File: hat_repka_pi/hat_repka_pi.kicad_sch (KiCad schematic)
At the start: 3 parts, among them Q1 BD233

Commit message: Добавлены основные компоненты на плату
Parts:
- removed C1: C_Small, symbol Device:C_Small
- removed Q1: BD233, Package_TO_SOT_THT:TO-126-3_Vertical, symbol Transistor_BJT:BD233
- removed R1: R, symbol Device:R
- added DS1: MT-12864J-2VLW-3V0, Display:MT-12864J-2VLW-3V0, symbol Melt:MT-12864J-2VLW-3V0
- added J1: Repka_Pi_3_type_piout_1, symbol Repka-Pi3:Repka_Pi_3_type_piout_1
- added Q1: 2SC1815, Package_TO_SOT_THT:TO-92_Inline, symbol Transistor_BJT:2SC1815
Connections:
- new net: DS1.1 (3.3V), DS1.20 (LEDK/EL), J1.1 (3V3)
- new net: DS1.10 (DB6), J1.19 (PC0/64/GPIO)
- new net: DS1.11 (DB7), J1.21 (PC1/65/GPIO)
- new net: DS1.12 (~{CS1}), J1.23 (PC2/66/GPIO)
- new net: DS1.13 (~{CS2}), J1.27 (PA19/19/GPIO)
- new net: DS1.14 (~{RST}), J1.29 (PA0/0/GPIO)
- new net: DS1.15 (R/~{W}), DS1.19 (LEDA/EL), DS1.2 (GND), J1.6 (GND)
- new net: DS1.16 (D/~{I}), J1.31 (PA1/1/GPIO)
- new net: DS1.17 (E), J1.33 (PL10/362/GPIO)
- new net: DS1.4 (DB0), J1.3 (PA12/12/GPIO)
- new net: DS1.5 (DB1), J1.5 (PA11/11/GPIO)
- new net: DS1.6 (DB2), J1.7 (PA7/7/GPIO)
- new net: DS1.7 (DB3), J1.11 (PA8/8/GPIO)
- new net: DS1.8 (DB4), J1.13 (PA9/9/GPIO)
- new net: DS1.9 (DB5), J1.15 (PA10/10/GPIO)

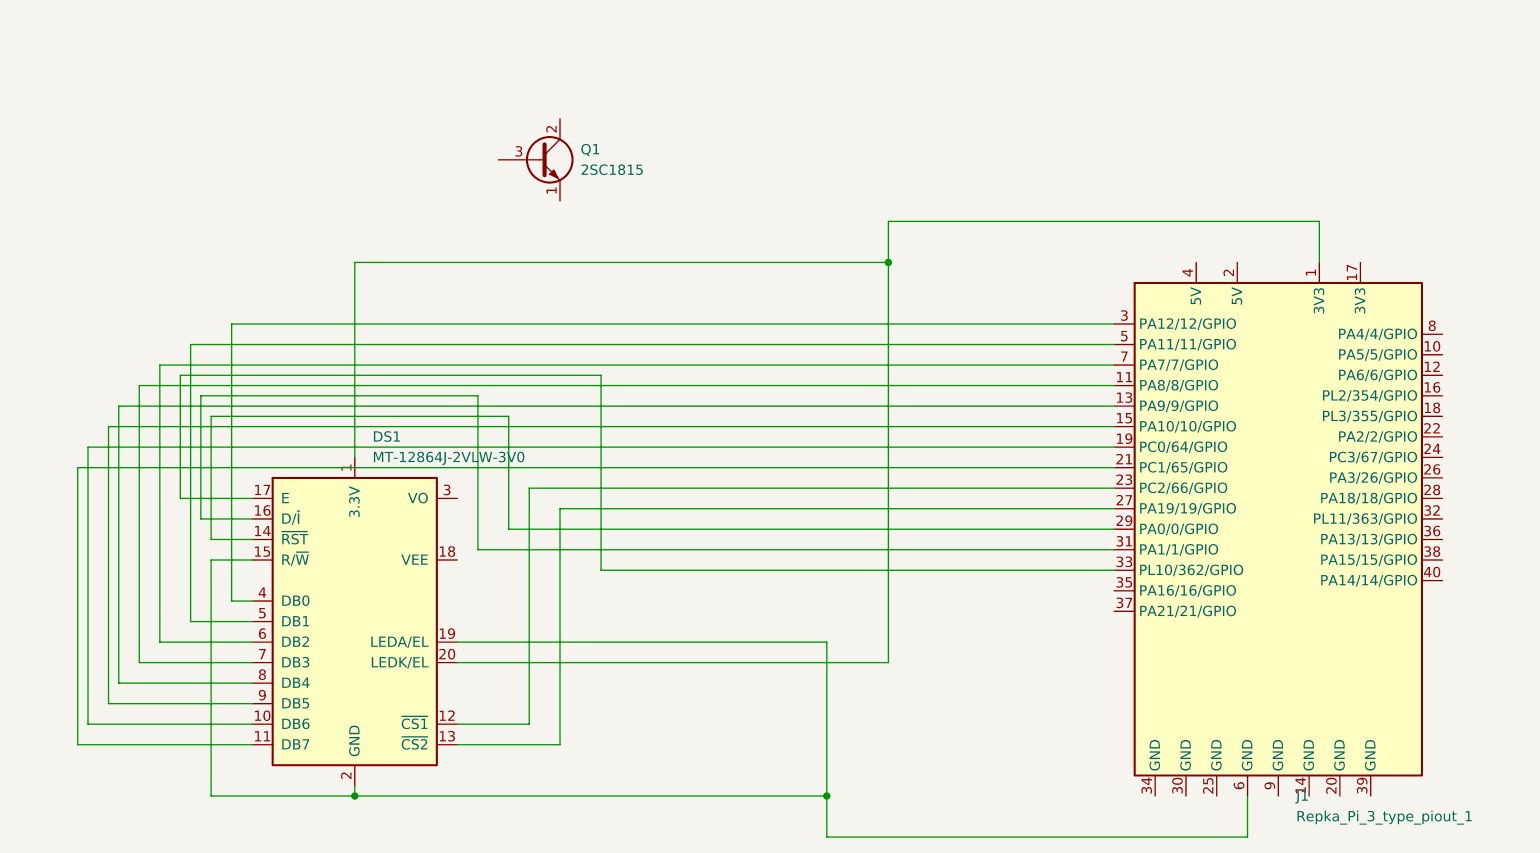
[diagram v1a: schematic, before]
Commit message: // Добавлена возможность подключить внешний дисплей ks0108 с паралельным интерфейсом
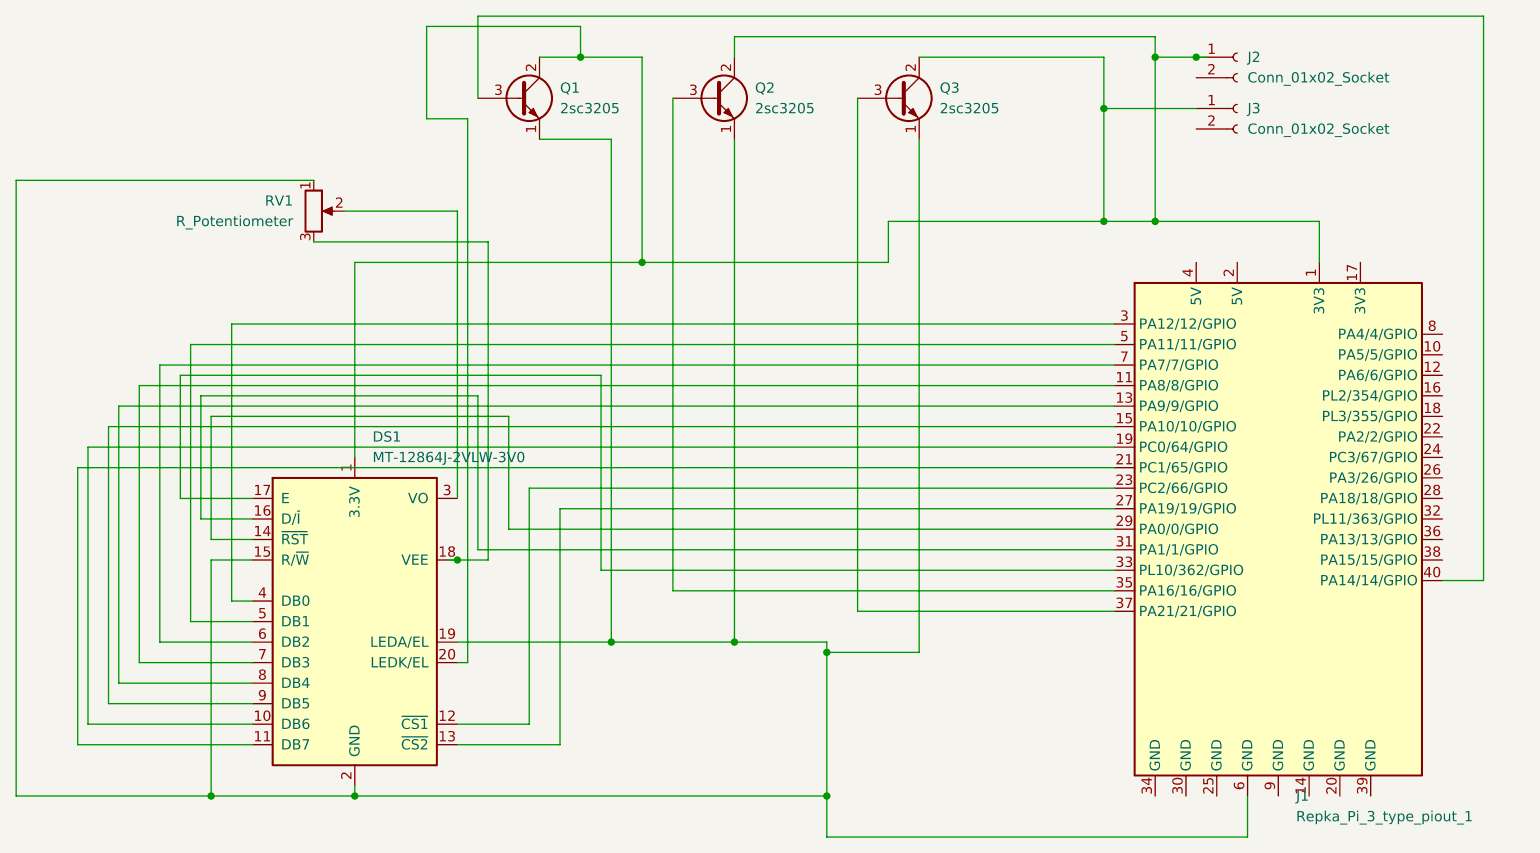
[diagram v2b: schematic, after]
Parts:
- removed Q1: 2SC1815, Package_TO_SOT_THT:TO-92_Inline, symbol Transistor_BJT:2SC1815
- added J2: Conn_01x02_Socket, Connector_PinSocket_2.54mm:PinSocket_1x02_P2.54mm_Vertical, symbol Connector:Conn_01x02_Socket
- added J3: Conn_01x02_Socket, symbol Connector:Conn_01x02_Socket
- added Q1, Q2, Q3: 2sc3205, Package_TO_SOT_THT:TO-92_Inline, symbol Other:2SC1815
- added RV1: R_Potentiometer, Potentiometer_THT:Potentiometer_Bourns_3296Y_Vertical, symbol Device:R_Potentiometer
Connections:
- net at DS1.1 (3.3V), DS1.20 (LEDK/EL), J1.1 (3V3): now also J2.1 (Pin_1), J3.1 (Pin_1), Q1.2 (C), Q2.2 (C), Q3.2 (C)
- net at DS1.15 (R/~{W}), DS1.19 (LEDA/EL), DS1.2 (GND)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: now also Q1.1 (E), Q2.1 (E), Q3.1 (E), RV1.1
- net at DS1.18 (VEE): now also RV1.3
- net at DS1.3 (VO): now also RV1.2
- net at J1.35 (PA16/16/GPIO): now also Q2.3 (B)
- net at J1.37 (PA21/21/GPIO): now also Q3.3 (B)
- net at J1.40 (PA14/14/GPIO): now also Q1.3 (B)
